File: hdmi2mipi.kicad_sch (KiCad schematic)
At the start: 1 part

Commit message: Add RP2040, fix pinout, add transistors for controlling the 1.8v and 3.3v outputs on the MIPI connector
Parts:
- added C1, C15, C2: 22p, Capacitor_SMD:C_0402_1005Metric, symbol mch2021-rescue:C-Device
- added C10, C11, C12, C13, C14, C4, C5, C6, C7: 100n, Capacitor_SMD:C_0402_1005Metric, symbol mch2021-rescue:C-Device
- added C16, C17, C8: 22u, Capacitor_SMD:C_0805_2012Metric, symbol mch2021-rescue:C-Device
- added C3, C9: 1u, Capacitor_SMD:C_0402_1005Metric, symbol mch2021-rescue:C-Device
- added C6: ~, symbol Device:C_Small
- added D1, D2, D3, D4, D5: LED, LED_SMD:LED_0603_1608Metric, symbol Device:LED
- added H1, H2, H3, H4: MountingHole_Pad, MountingHole:MountingHole_2.2mm_M2_Pad_Via, symbol Mechanical:MountingHole_Pad
- added J10: BOOT, Connector_PinHeader_2.54mm:PinHeader_1x02_P2.54mm_Vertical, symbol Connector_Generic:Conn_01x02
- added J11: USB_C_Receptacle_USB2.0, Connector_USB:USB_C_Receptacle_HRO_TYPE-C-31-M-12, symbol Connector:USB_C_Receptacle_USB2.0
- added J2: HDMI_A_1.4, symbol Connector:HDMI_A_1.4
- added J3: ~, symbol tc358870xbg:Conn_01x60_mipi_pinout
- added J6: QWIIC, symbol Connector_Generic_MountingPin:Conn_01x04_MountingPin
- added J7: SWD, Connector_JST:JST_SH_SM03B-SRSS-TB_1x03-1MP_P1.00mm_Horizontal, symbol Connector_Generic_MountingPin:Conn_01x03_MountingPin
- added J7: TP, Connector_JST:JST_SH_SM07B-SRSS-TB_1x07-1MP_P1.00mm_Horizontal, symbol Connector_Generic_MountingPin:Conn_01x07_MountingPin
- added L1: 2.2u, custom:Inductor_MSC20FC, symbol mch2021-rescue:L-Device
- added Q1, Q2, Q3 (x4): BC846, Package_TO_SOT_SMD:SOT-23, symbol Transistor_BJT:BC846
- added R10, R11, R12, R13, R18, R5, R8, R9: 1k, Resistor_SMD:R_0402_1005Metric, symbol mch2021-rescue:R-Device
- added R10: 2k, symbol Device:R_Small
- added R11: 48k, symbol Device:R_Small
- added R12: 0, symbol Device:R_Small
- added R13: 1.5k, symbol Device:R_Small
- added R14, R15: 5.1k, Resistor_SMD:R_0402_1005Metric, symbol mch2021-rescue:R-Device
- added R14, R20, R21, R23, R24, R25, R26, R27, R28, R29, R41, R43, R45, R47, R48: 4.7k, symbol Device:R_Small
- added R15, R38, R39, R40, R42, R44, R46, R49, R50: 10k, symbol Device:R_Small
- added R16, R17, R37: 33, symbol Device:R_Small
- added R16: 10k, Resistor_SMD:R_0402_1005Metric, symbol mch2021-rescue:R-Device
- added R17: 45.3k, Resistor_SMD:R_0402_1005Metric, symbol mch2021-rescue:R-Device
- added R18, R19: 1k, symbol Device:R_Small
- added R22: 100k, symbol Device:R_Small
- added R5 (x2): 100, Resistor_SMD:R_0402_1005Metric, symbol mch2021-rescue:R-Device
- added R6, R7: 27, Resistor_SMD:R_0402_1005Metric, symbol mch2021-rescue:R_Small-Device
- added U1: RP2040, custom:QFN40P700X700X90-57N, symbol RP2040:RP2040
- added U2: W25Q16JVUXIQ, custom:PSON50P300X200X60-9N, symbol mch2021-rescue:SPIFLASH_QSPI-spiflash
- added U3: W25Q16JVUXIQ, Package_SO:SOIC-8_5.23x5.23mm_P1.27mm, symbol mch2021-rescue:SPIFLASH_QSPI-spiflash
- added U3 (x2): SY6280AAC, Package_TO_SOT_SMD:SOT-23-5, symbol symbols:AAT4610BIGV-1-T1-Power_Management
- added U4: PCA9306DC, Package_SO:VSSOP-8_2.3x2mm_P0.5mm, symbol Interface:PCA9306DC
- added U4: SY8079AAC, Package_TO_SOT_SMD:SOT-23-5, symbol mch2021-rescue:TLV62568DBV-Regulator_Switching
- added X2: SG-210STF, Oscillator:Oscillator_SMD_SeikoEpson_SG210-4Pin_2.5x2.0mm, symbol Oscillator:SG-210STF
- added Y1: 12MHz, Crystal:Crystal_SMD_3225-4Pin_3.2x2.5mm, symbol mch2021-rescue:Crystal_GND24_Small-Device
- renumbered U1 to U2
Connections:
- net VDDC11 is gone; now on net VDD11_HDMI: U2.C10 (VDDC11), U2.K6 (VDDC11)
- net GND: now also U2.G5 (TEST), C1.2, C10.2, C11.2, C12.2, C13.2, C14.2, C16.2, C17.2, C2.2, C3.2, C4.2, C5.2, C6.2, C6.2, C7.2, C8.2, C9.2, D1.1 (K), D2.1 (K), D3.1 (K), D4.1 (K), D5.1 (K), H1.1, H2.1, H3.1, H4.1, J10.1 (Pin_1), J11.A1 (GND), J11.A12 (GND), J11.B1 (GND), J11.B12 (GND), J11.S1 (SHIELD), J2.11 (CKS), J2.17 (GND), J2.2 (D2S), J2.5 (D1S), J2.8 (D0S), J2.SH, J3.1 (GND), J3.10 (GND), J3.13 (GND), J3.16 (GND), J3.19 (GND), J3.22 (GND), J3.25 (GND), J3.28 (GND), J3.31 (GND), J3.4 (GND), J3.44 (GND), J3.46 (GND), J3.49 (GND), J3.7 (GND), J6.1 (Pin_1), J6.MP (MountPin), J7.2 (Pin_2), J7.7 (Pin_7), J7.MP (MountPin), J7.MP (MountPin), Q1.2 (E), Q2.2 (E), Q3.2 (E), Q3.2 (E), Q3.2 (E), Q3.2 (E), R11.1, R14.1, R15.1, R16.2, R22.1, R23.2, R38.2, R39.2, R40.2, R42.2, R44.2, R46.2, R48.2, R49.2, R50.2, U1.19 (TESTEN), U1.57 (GND), U2.4 (VSS), U3.2 (GND), U3.2 (GND), U3.4 (VSS), U4.1 (GND), U4.2 (GND), X2.2 (GND), Y1.2, Y1.4
- net VDD33_HDMI: now also U2.H2 (VDDIO33), U2.J7 (VDDIO18), R10.2, R27.1, R29.1, U3.1 (OUT), X2.1 (~{ST}), X2.4 (Vcc)
- net at U2.A1 (REXT): now also R10.1
- net at U2.A2 (CEC): now also J2.13 (CEC)
- net at U2.A3 (DDC_SCL): now also R16.1
- net at U2.A4 (HPDI): now also R12.2, R13.1
- net at U2.A5 (CDSI1D3P): now also J3.3 (DSI1D3P)
- net at U2.A6 (CDSI1D2P): now also J3.6 (DSI1D2P)
- net at U2.A7 (CDSI1CP): now also J3.9 (DSI1CP)
- net at U2.A8 (CDSI1D1P): now also J3.12 (DSID1P)
- net at U2.A9 (CDSI1D0P): now also J3.15 (DSI1D0P)
- net MC_VSUPPLY_12: now reaches U2.B10 (VDD12_MIPI1)
- net MC_VSUPPLY_12: now also U2.J10 (VDD12_MIPI0)
- net at U2.B3 (DDC_SDA): now also R17.2
- net at U2.B4 (HPDO): now also R14.2, R18.1
- net at U2.B5 (CDSI1D3N): now also J3.2 (DSI1D3N)
- net at U2.B6 (CDSI1D2N): now also J3.5 (DSI1D2N)
- net at U2.B7 (CDSI1CN): now also J3.8 (DSI1CN)
- net at U2.B8 (CDSI1D1N): now also J3.11 (DSID1N)
- net at U2.B9 (CDSI1D0N): now also J3.14 (DSI1D0N)
- net at U2.C1 (HDMICP): now also J2.10 (CK+)
- net at U2.C2 (HDMICN): now also J2.12 (CK-)
- net at U2.D1 (HDMID0P): now also J2.7 (D0+)
- net at U2.D10 (CDSI0D3P): now also J3.18 (DSI0D3P)
- net at U2.D2 (HDMID0N): now also J2.9 (D0-)
- net at U2.D9 (CDSI0D3N): now also J3.17 (DSI0D3N)
- net at U2.E1 (HDMID1P): now also J2.4 (D1+)
- net at U2.E10 (CDSI0D2P): now also J3.21 (DSI0D2P)
- net at U2.E2 (HDMID1N): now also J2.6 (D1-)
- net at U2.E9 (CDSI0D2N): now also J3.20 (DSI0D2N)
- net at U2.F1 (HDMID2P): now also J2.1 (D2+)
- net at U2.F10 (CDSI0CP): now also J3.24 (DSI0CP)
- net at U2.F2 (HDMID2N): now also J2.3 (D2-)
- net at U2.F9 (CDSI0CN): now also J3.23 (DSI0CN)
- net at U2.G10 (CDSI0D1P): now also J3.27 (DSI0D1P)
- net at U2.G9 (CDSI0D1N): now also J3.26 (DSI0D1N)
- net at U2.H10 (CDSI0D0P): now also J3.30 (DSI0D0P)
- net at U2.H9 (CDSI0D0N): now also J3.29 (DSI0D0N)
- net at U2.J3 (INT): now also R40.1, U1.40 (GPIO28/ADC2)
- net at U2.K3 (I2C_SDA): now also R29.2, U1.36 (GPIO24)
- net at U2.K4 (I2C_SCL): now also R27.2, U1.37 (GPIO25)
- net at U2.K8 (~{RESET}): now also R38.1, U1.39 (GPIO27/ADC1)
- net at U2.K9 (REFCLK): now also R37.2
- new net: D4.2 (A), R12.2
- new net: J2.18 (+5V), R12.1, R15.1, R20.1, R21.1, R22.2
- new net: Q1.3 (C), Q2.1 (B), R15.2
- new net: J7.3 (Pin_3), R24.2, U4.3 (SCL1)
- new net: C2.1, R5.1, Y1.3
- new net: J2.19 (HPD/HEAC-), Q2.3 (C), R18.2, R19.1
- new net: D2.2 (A), R10.2
- new net: J2.15 (SCL), R16.2, R21.2
- new net: Q1.1 (B), R14.1
- new net: C6.1, R11.2, R13.2, R19.2
- new net: J7.4 (Pin_4), R25.2, U4.4 (SDA1)
- new net: J6.3 (Pin_3), R26.2, U1.34 (GPIO22), U4.5 (SDA2)
- new net: J6.4 (Pin_4), R28.2, U1.35 (GPIO23), U4.6 (SCL2)
- new net: J11.A7 (D-), J11.B7 (D-), R6.1
- new net: R6.2, U1.46 (USB_DM)
- new net: D1.2 (A), R9.2
- new net: R49.1, U1.5 (GPIO3), U3.4 (ON)
- new net: J7.1 (Pin_1), R5.1
- new net: J7.3 (Pin_3), R5.1
- new net: Q3.1 (B), R46.1, U1.3 (GPIO1)
- new net: J3.41 (1.8-S1), Q3.3 (C), R47.2
- new net: R48.1, U3.3 (SET)
- new net: R50.1, U1.38 (GPIO26/ADC0), U3.4 (ON)
- new net: D5.2 (A), R13.2
- new net: Q3.1 (B), R44.1, U1.4 (GPIO2)
- new net: J3.33 (3.3-S1), Q3.3 (C), R43.2
- new net: J3.34 (3.3-S2), Q3.3 (C), R41.2
- new net: J3.36 (3.3v), J3.37 (3.3v), R41.1, R43.1, U3.1 (OUT)
- new net: J3.39 (1.8v), R45.1, R47.1
- new net: J3.42 (1.8-S2), Q3.3 (C), R45.2
- new net: J3.51 (LED+), J3.52 (LED+), J3.53 (LED+)
- new net: J3.55 (FB2), J3.56 (FB2)
- new net: J3.59 (FB1), J3.60 (FB1)
- new net: J2.16 (SDA), R17.1, R20.2
- new net: R5.2, U1.25 (SWD)
- new net: J11.A5 (CC1), R14.2
- new net: Q3.1 (B), R39.1, U1.7 (GPIO5)
- new net: D3.2 (A), R11.2
- new net: R18.1, U1.26 (RUN)
- new net: R5.2, U1.24 (SWCLK)
- new net: R7.1, U1.47 (USB_DP)
- new net: Q3.1 (B), R42.1, U1.6 (GPIO4)
- new net: R23.1, U3.3 (SET)
- new net: J11.A6 (D+), J11.B6 (D+), R7.2
- new net: J11.B5 (CC2), R15.2
- new net: R37.1, X2.3 (OUT)
- new net +3V3: C10.1, C12.1, C14.1, C15.1, C16.1, C17.1, C3.1, C4.1, C5.1, C7.1, J6.2 (Pin_2), L1.1, R17.1, R18.2, R26.1, R28.1, U1.1 (IOVDD), U1.10 (IOVDD), U1.22 (IOVDD), U1.33 (IOVDD), U1.42 (IOVDD), U1.43 (ADC_AVDD), U1.44 (VREG_VIN), U1.48 (USB_VDD), U1.49 (IOVDD), U2.8 (VDD), U3.5 (IN), U3.5 (IN), U3.8 (VDD), U4.7 (VREF2), U4.8 (EN)
- new net FB33: C15.2, R16.1, R17.2, U4.5 (FB)
- new net RP_BTN: J10.2 (Pin_2), R8.2
- new net RP_QSPI_CSN: R8.1, U1.56 (QSPI_CSN), U2.1 (~{CS}), U3.1 (~{CS})
- new net RP_QSPI_SCLK: U1.52 (QSPI_SCLK), U2.6 (SCK), U3.6 (SCK)
- new net RP_QSPI_SD0: U1.53 (QSPI_SD0), U2.5 (MOSI/IO0), U3.5 (MOSI/IO0)
- new net RP_QSPI_SD1: U1.55 (QSPI_SD1), U2.2 (MISO/IO1), U3.2 (MISO/IO1)
- new net RP_QSPI_SD2: U1.54 (QSPI_SD2), U2.3 (IO2), U3.3 (IO2)
- new net RP_QSPI_SD3: U1.51 (QSPI_SD3), U2.7 (IO3), U3.7 (IO3)
- new net RP_XIN: C1.1, U1.20 (XIN), Y1.1
- new net RP_XOUT: R5.2, U1.21 (XOUT)
- new net SW33: L1.2, U4.3 (SW)
- new net TP_INT: J7.1 (Pin_1)
- new net TP_RST: J7.2 (Pin_2)
- new net TP_VSUPPLY_18: J7.5 (Pin_5), R24.1, R25.1, U4.2 (VREF1)
- new net TP_VSUPPLY_33: J7.6 (Pin_6)
- new net VIN: C6.1, C8.1, J11.A4 (VBUS), J11.A9 (VBUS), J11.B4 (VBUS), J11.B9 (VBUS), J3.35 (5v), U4.1 (EN), U4.4 (VIN)
- new net rpi_1.1v: C11.1, C13.1, C9.1, U1.23 (DVDD), U1.45 (VREG_VOUT), U1.50 (DVDD)
- no-connect marks 0 -> 11
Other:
- note added: "1.8v"
- note added: "100k pulldown to pull SDA/SCL low when HDMI is disconnected"
- note added: "3.3v"
- note added: "5v"
- note added: "?"
- note added: "GND"
- note added: "I2C0 SDA I2C0 SCL"
- note added: "I2C1 SDA I2C1 SCL"
- note added: "No clue yet how these are supposed to work"
- note added: "Place close to chip"
- note added: "Place close to pin 44"
- note added: "Place close to pin 45"
- note added: "Pulldown on INT: I2C address is 0x0F"
- note added: "SPI0 SCK SPI0 TX SPI0 RX"
- note added: "SPI1 SCK SPI1 TX SPI1 RX"
- note added: "To-do: add 1.8v DC-DC"
- note added: "UART0 TX UART0 RX UART0 CTS UART0 RTS"
- note added: "UART1 TX UART1 RX UART1 CTS UART1 RTS"
- company: (none) -> Nicolai Electronics
- title: (none) -> HDMI to MIPI converter

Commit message: Most of schematic done, experimenting with component placement
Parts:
- removed U3: SY6280AAC, Package_TO_SOT_SMD:SOT-23-5, symbol symbols:AAT4610BIGV-1-T1-Power_Management
- added C1: 1u, Capacitor_SMD:C_0402_1005Metric, symbol mch2021-rescue:C-Device
- added C14, C33, C4: 100n, Capacitor_SMD:C_0402_1005Metric, symbol Device:C_Small
- added C15 (x3): 22p, Capacitor_SMD:C_0402_1005Metric, symbol mch2021-rescue:C-Device
- added C16 (x3), C17 (x3), C8 (x4): 22u, Capacitor_SMD:C_0805_2012Metric, symbol mch2021-rescue:C-Device
- added C3, C6 (x7): 100n, Capacitor_SMD:C_0402_1005Metric, symbol mch2021-rescue:C-Device
- added C39, C43: 1n, Capacitor_SMD:C_0402_1005Metric, symbol Device:C_Small
- added C40, C41: 0.1u, Capacitor_SMD:C_0402_1005Metric, symbol Device:C_Small
- added C42: 5p, Capacitor_SMD:C_0402_1005Metric, symbol Device:C_Small
- added C47 (x2): 39n, Capacitor_SMD:C_0402_1005Metric, symbol Device:C_Small
- added C5, C6: 47u, Capacitor_SMD:C_0805_2012Metric, symbol Device:C_Small
- added J1: AudioJack3, custom:Boom-audiojack-PJ-320B, symbol mch2021-rescue:AudioJack3-Connector
- added L1 (x3): 2.2u, custom:Inductor_MSC20FC, symbol mch2021-rescue:L-Device
- added Q7: 2SC2712, Package_TO_SOT_SMD:SOT-23, symbol Device:Q_NPN_BEC
- added R16 (x6), R17: 10k, Resistor_SMD:R_0402_1005Metric, symbol mch2021-rescue:R-Device
- added R17: 20k, Resistor_SMD:R_0402_1005Metric, symbol mch2021-rescue:R-Device
- added R17: 8.2k, Resistor_SMD:R_0402_1005Metric, symbol mch2021-rescue:R-Device
- added R27, R28: 330, Resistor_SMD:R_0402_1005Metric, symbol mch2021-rescue:R-Device
- added R60: 1k, Resistor_SMD:R_0402_1005Metric, symbol Device:R_Small
- added U1: MS4344, custom:SOP50P490X110-10N, symbol CS4344-CZZ:CS4344-CZZ
- added U4 (x3): SY8079AAC, Package_TO_SOT_SMD:SOT-23-5, symbol mch2021-rescue:TLV62568DBV-Regulator_Switching
- C6: footprint (none) -> Capacitor_SMD:C_0402_1005Metric
- J2: footprint (none) -> Connector_HDMI:HDMI_A_Molex_208658-1001_Horizontal
- J3: footprint (none) -> fpc60:Hirose_FH52-60S-0.5SH_1x60-1MP_P0.50mm_Horizontal
- J5: renamed from J6; footprint (none) -> Connector_JST:JST_SH_SM04B-SRSS-TB_1x04-1MP_P1.00mm_Horizontal
- R10, R11, R12, R13, R14, R15, R16, R17, R18, R19, R20, R21, R22, R23, R24, R25, R26, R27, R28, R29, R37, R38, R39, R40, R41, R42, R43, R44, R45, R46, R47, R50: footprint (none) -> Resistor_SMD:R_0402_1005Metric
- R48: value 4.7k -> 1k; footprint (none) -> Resistor_SMD:R_0402_1005Metric
- R49: value 10k -> 1.5k; footprint (none) -> Resistor_SMD:R_0402_1005Metric
- renumbered J7 to J4, Q3 to Q4, Q3 to Q5, Q3 to Q6
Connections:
- net TP_VSUPPLY_18 is gone; now on net +1V8: J4.5 (Pin_5), R24.1, R25.1, U4.2 (VREF1)
- net TP_VSUPPLY_33 is gone; now on net VDD33_HDMI: J4.6 (Pin_6)
- net +3V3: now also C1.1, C3.1, U1.9 (VA)
- net GND: now also J3.12 (GND), J3.15 (GND), J3.17 (GND), J3.30 (GND), J3.33 (GND), J3.36 (GND), J3.39 (GND), J3.42 (GND), J3.45 (GND), J3.48 (GND), J3.51 (GND), J3.54 (GND), J3.57 (GND), J3.60 (GND), J3.MP, C1.2, C16.2, C16.2, C16.2, C17.2, C17.2, C17.2, C3.2, C39.2, C4.2, C40.2, C47.1, C47.1, C5.2, C6.2, C6.2, C6.2, C6.2, C6.2, C6.2, C6.2, C6.2, C8.2, C8.2, C8.2, C8.2, J1.S, R16.2, R16.2, R16.2, R16.2, R16.2, R16.2, U1.8 (GND), U4.2 (GND), U4.2 (GND), U4.2 (GND); no longer J3.1 (GND), J3.10 (GND), J3.13 (GND), J3.16 (GND), J3.19 (GND), J3.22 (GND), J3.25 (GND), J3.28 (GND), J3.31 (GND), J3.4 (GND), J3.44 (GND), J3.46 (GND), J3.49 (GND), J3.7 (GND), R48.2, R49.2
- net VDD33_HDMI: now also J3.24 (3.3v), J3.25 (3.3v), R41.1, R43.1, C6.1, C6.1, C8.1, Q7.3 (C)
- net VIN: now also J3.26 (5v); no longer C6.1, C8.1, J11.A4 (VBUS), J11.A9 (VBUS), J11.B4 (VBUS), J11.B9 (VBUS), J3.35 (5v), U4.1 (EN), U4.4 (VIN)
- net at J3.3: no longer U2.A5 (CDSI1D3P)
- net at J3.6 (FB2): now also J3.5 (FB2); no longer U2.A6 (CDSI1D2P)
- net at J3.9 (LED+): now also J3.10 (LED+), J3.8 (LED+); no longer U2.A7 (CDSI1CP)
- net DSI1_D1_P: now reaches U2.A8 (CDSI1D1P)
- net DSI1_D1_P: now also J3.49 (DSID1P); no longer J3.12 (DSID1P)
- net DSI1_D0_P: now reaches U2.A9 (CDSI1D0P)
- net DSI1_D0_P: now also J3.46 (DSI1D0P); no longer J3.15 (DSI1D0P)
- net at J3.2 (FB1): now also J3.1 (FB1); no longer U2.B5 (CDSI1D3N)
- net DSI1_D2_N: now reaches U2.B6 (CDSI1D2N)
- net DSI1_D2_N: now also J3.56 (DSI1D2N); no longer J3.5 (DSI1D2N)
- net DSI1_C_N: now reaches U2.B7 (CDSI1CN)
- net DSI1_C_N: now also J3.53 (DSI1CN); no longer J3.8 (DSI1CN)
- net at J3.11: no longer U2.B8 (CDSI1D1N)
- net at J3.14 (5.8v-VDD): no longer U2.B9 (CDSI1D0N)
- net HDMI_C_P: now reaches J2.10 (CK+), U2.C1 (HDMICP)
- net HDMI_C_N: now reaches J2.12 (CK-), U2.C2 (HDMICN)
- net HDMI_0_P: now reaches J2.7 (D0+), U2.D1 (HDMID0P)
- net at J3.18: no longer U2.D10 (CDSI0D3P)
- net HDMI_0_N: now reaches J2.9 (D0-), U2.D2 (HDMID0N)
- net DSI0_D3_N: now reaches U2.D9 (CDSI0D3N)
- net DSI0_D3_N: now also J3.44 (DSI0D3N); no longer J3.17 (DSI0D3N)
- net HDMI_1_P: now reaches J2.4 (D1+), U2.E1 (HDMID1P)
- net at J3.21: no longer U2.E10 (CDSI0D2P)
- net HDMI_1_N: now reaches J2.6 (D1-), U2.E2 (HDMID1N)
- net at J3.20 (1.8-S1): now also Q6.3 (C), R47.2; no longer U2.E9 (CDSI0D2N)
- net HDMI_2_P: now reaches J2.1 (D2+), U2.F1 (HDMID2P)
- net DSI0_C_P: now reaches U2.F10 (CDSI0CP)
- net DSI0_C_P: now also J3.37 (DSI0CP); no longer J3.24 (DSI0CP)
- net HDMI_2_N: now reaches J2.3 (D2-), U2.F2 (HDMID2N)
- net at J3.23: no longer U2.F9 (CDSI0CN)
- net at J3.27 (3.3-S2): now also Q3.3 (C), R41.2; no longer U2.G10 (CDSI0D1P)
- net DSI0_D1_N: now reaches U2.G9 (CDSI0D1N)
- net DSI0_D1_N: now also J3.35 (DSI0D1N); no longer J3.26 (DSI0D1N)
- net DSI0_D0_P: now reaches U2.H10 (CDSI0D0P)
- net DSI0_D0_P: now also J3.31 (DSI0D0P); no longer J3.30 (DSI0D0P)
- net at J3.29: no longer U2.H9 (CDSI0D0N)
- net at U2.J1 (BIASDA): now also C41.2
- net at U2.J2 (DAOUT): now also R49.2
- net at U2.J4 (A_OSCK): now also U1.4 (MCLK)
- net at U2.J9 (A_SD0): now also U1.1 (SDIN)
- net at U2.K1 (PCKIN): now also C43.2
- net at U2.K2 (PFIL): now also R48.1, C39.1
- net at U2.K5 (A_WFS): now also U1.3 (LRCK)
- net at U2.K7 (A_SCK): now also U1.2 (~{DEM}/SCLK)
- net at R10.1: now also U1.14 (GPIO11)
- net at R49.1: now also C42.1, Q7.1 (B); no longer U1.5 (GPIO3)
- net 1V8_S1: now reaches Q6.1 (B), R46.1
- net 1V8_S1: now also U1.2 (GPIO0); no longer U1.3 (GPIO1)
- net 1V8_S2: now reaches Q5.1 (B), R44.1
- net 1V8_S2: now also U1.3 (GPIO1); no longer U1.4 (GPIO2)
- net DSI0_D0_N: now reaches J3.32 (DSI0D0N)
- net DSI0_D0_N: now also U2.H9 (CDSI0D0N)
- net at Q4.3 (C), R43.2: now also J3.28 (3.3-S1); no longer J3.33 (3.3-S1)
- net DSI0_C_N: now reaches J3.38 (DSI0CN)
- net DSI0_C_N: now also U2.F9 (CDSI0CN)
- net +1V8: now reaches R45.1, R47.1
- net +1V8: now also J3.22 (1.8v), C15.1, C16.1, C17.1, L1.1, R17.1; no longer J3.39 (1.8v)
- net DSI0_D2_P: now reaches J3.40 (DSI0D2P)
- net DSI0_D2_P: now also U2.E10 (CDSI0D2P)
- net at Q5.3 (C), R45.2: now also J3.19 (1.8-S2); no longer J3.42 (1.8-S2)
- net DSI0_D3_P: now reaches J3.43 (DSI0D3P)
- net DSI0_D3_P: now also U2.D10 (CDSI0D3P)
- net DSI1_D0_N: now reaches J3.47 (DSI1D0N)
- net DSI1_D0_N: now also U2.B9 (CDSI1D0N)
- net DSI1_D1_N: now reaches J3.50 (DSID1N)
- net DSI1_D1_N: now also U2.B8 (CDSI1D1N)
- net DSI1_D2_P: now reaches J3.55 (DSI1D2P)
- net DSI1_D2_P: now also U2.A6 (CDSI1D2P); no longer J3.56 (FB2)
- net DSI1_D3_P: now reaches J3.58 (DSI1D3P)
- net DSI1_D3_P: now also U2.A5 (CDSI1D3P)
- net DSI1_D3_N: now reaches J3.59 (DSI1D3N)
- net DSI1_D3_N: now also U2.B5 (CDSI1D3N); no longer J3.60 (FB1)
- net at R12.1: now also U1.16 (GPIO13)
- net 3V3_S2: now reaches Q3.1 (B), R39.1
- net 3V3_S2: now also U1.5 (GPIO3); no longer U1.7 (GPIO5)
- net at R11.1: now also U1.15 (GPIO12)
- net at U1.13 (GPIO10): now also R9.1
- net at U1.17 (GPIO14): now also R13.1
- net 1V1_EN: now reaches U1.18 (GPIO15)
- net 1V1_EN: now also R16.1, U4.1 (EN)
- net 1V2_EN: now reaches U1.27 (GPIO16)
- net 1V2_EN: now also R16.1, U4.1 (EN)
- net 1V8_EN: now reaches U1.28 (GPIO17)
- net 1V8_EN: now also R16.1, U4.1 (EN)
- net 3V3_S1: now reaches Q4.1 (B), R42.1
- net 3V3_S1: now also U1.4 (GPIO2); no longer U1.6 (GPIO4)
- net MC_VSUPPLY_12 renamed +1V2
- net +1V2: now also C15.1, C16.1, C17.1, C6.1, L1.1, R17.1
- net VDD11_HDMI renamed +1V1
- net +1V1: now also C15.1, C16.1, C17.1, C6.1, L1.1, R17.1
- new net: C5.1, U1.6 (FILT+)
- new net: C4.1, C6.1, U1.5 (VQ)
- new net: C33.1, U1.10 (AOUTR)
- new net: C33.2, R28.1
- new net: C43.1, Q7.2 (E), R60.2
- new net: C41.1, C42.2, R60.1
- new net: C40.1, R48.2
- new net: C14.2, U1.7 (AOUTL)
- new net: C14.1, R27.1
- new net AUDIO_L: C47.2, J1.T, R27.2
- new net AUDIO_R: C47.2, J1.R, R28.2
- new net DSI0_D1_P: J3.34 (DSI0D1P), U2.G10 (CDSI0D1P)
- new net DSI0_D2_N: J3.41 (DSI0D2N), U2.E9 (CDSI0D2N)
- new net DSI1_C_P: J3.52 (DSI1CP), U2.A7 (CDSI1CP)
- new net FB11: C15.2, R16.1, R17.2, U4.5 (FB)
- new net FB12: C15.2, R16.1, R17.2, U4.5 (FB)
- new net FB18: C15.2, R16.1, R17.2, U4.5 (FB)
- new net SW11: L1.2, U4.3 (SW)
- new net SW12: L1.2, U4.3 (SW)
- new net SW18: L1.2, U4.3 (SW)
- new net VBUS: C6.1, C6.1, C6.1, C6.1, C8.1, C8.1, C8.1, C8.1, J11.A4 (VBUS), J11.A9 (VBUS), J11.B4 (VBUS), J11.B9 (VBUS), U4.1 (EN), U4.4 (VIN), U4.4 (VIN), U4.4 (VIN), U4.4 (VIN)
- no-connect marks 11 -> 14
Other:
- added sheet Untitled Sheet (untitled.kicad_sch)
- note removed: "To-do: add 1.8v DC-DC"
- moved on the sheet: C15, C16, C17, C6, C8, D1, D2, D3, D4, D5, L1, Q3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

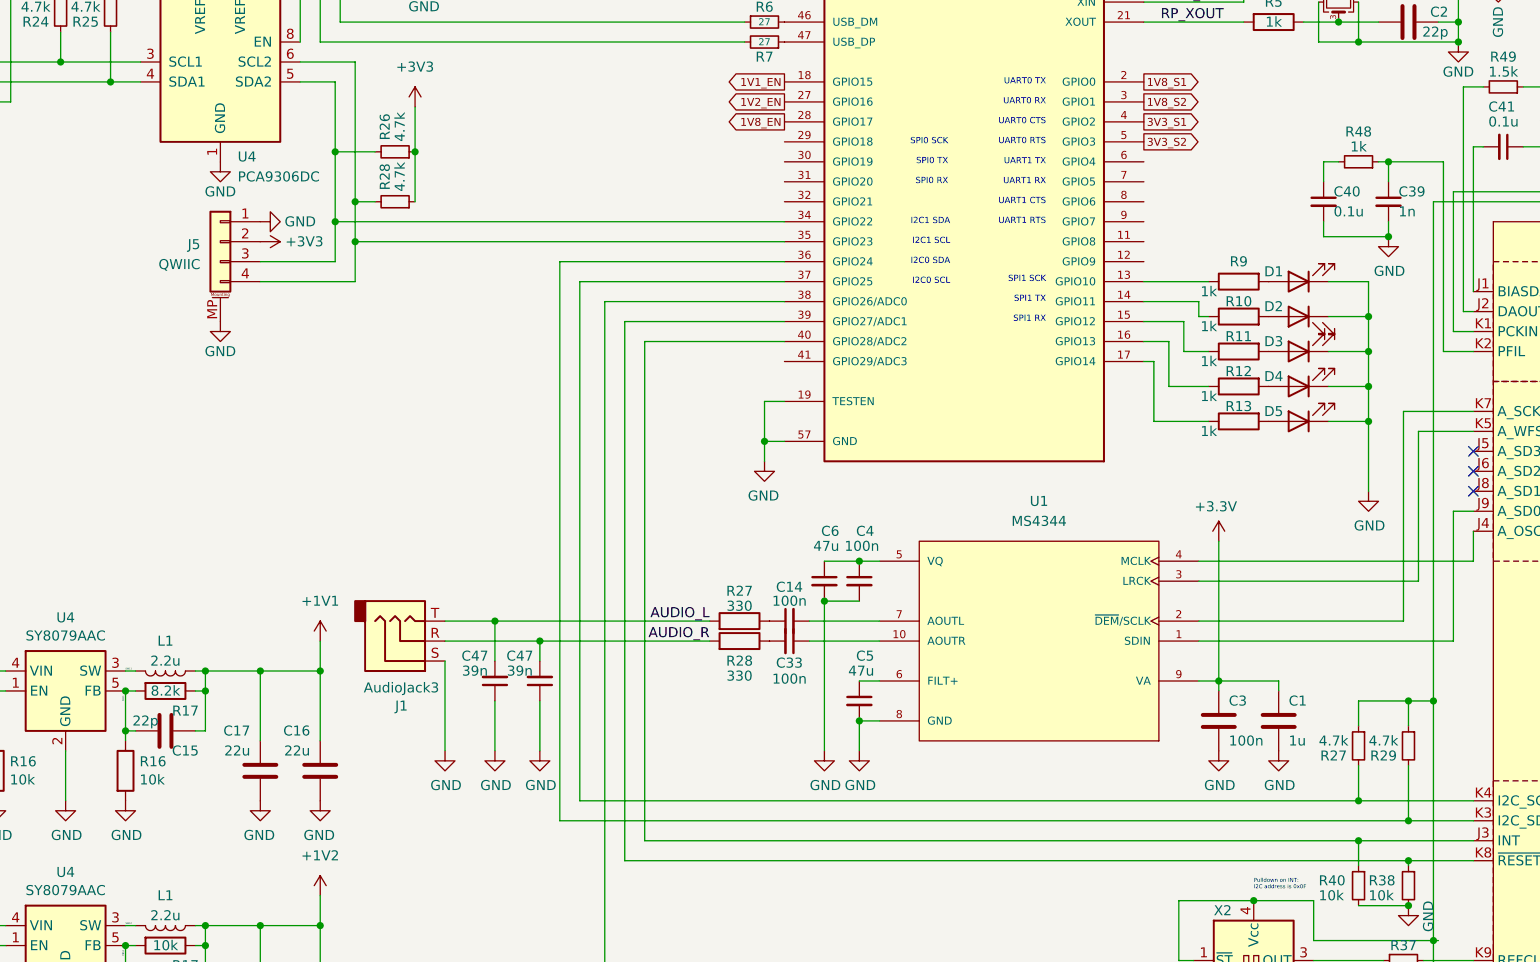
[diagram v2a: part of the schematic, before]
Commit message: Board to 7cm+-
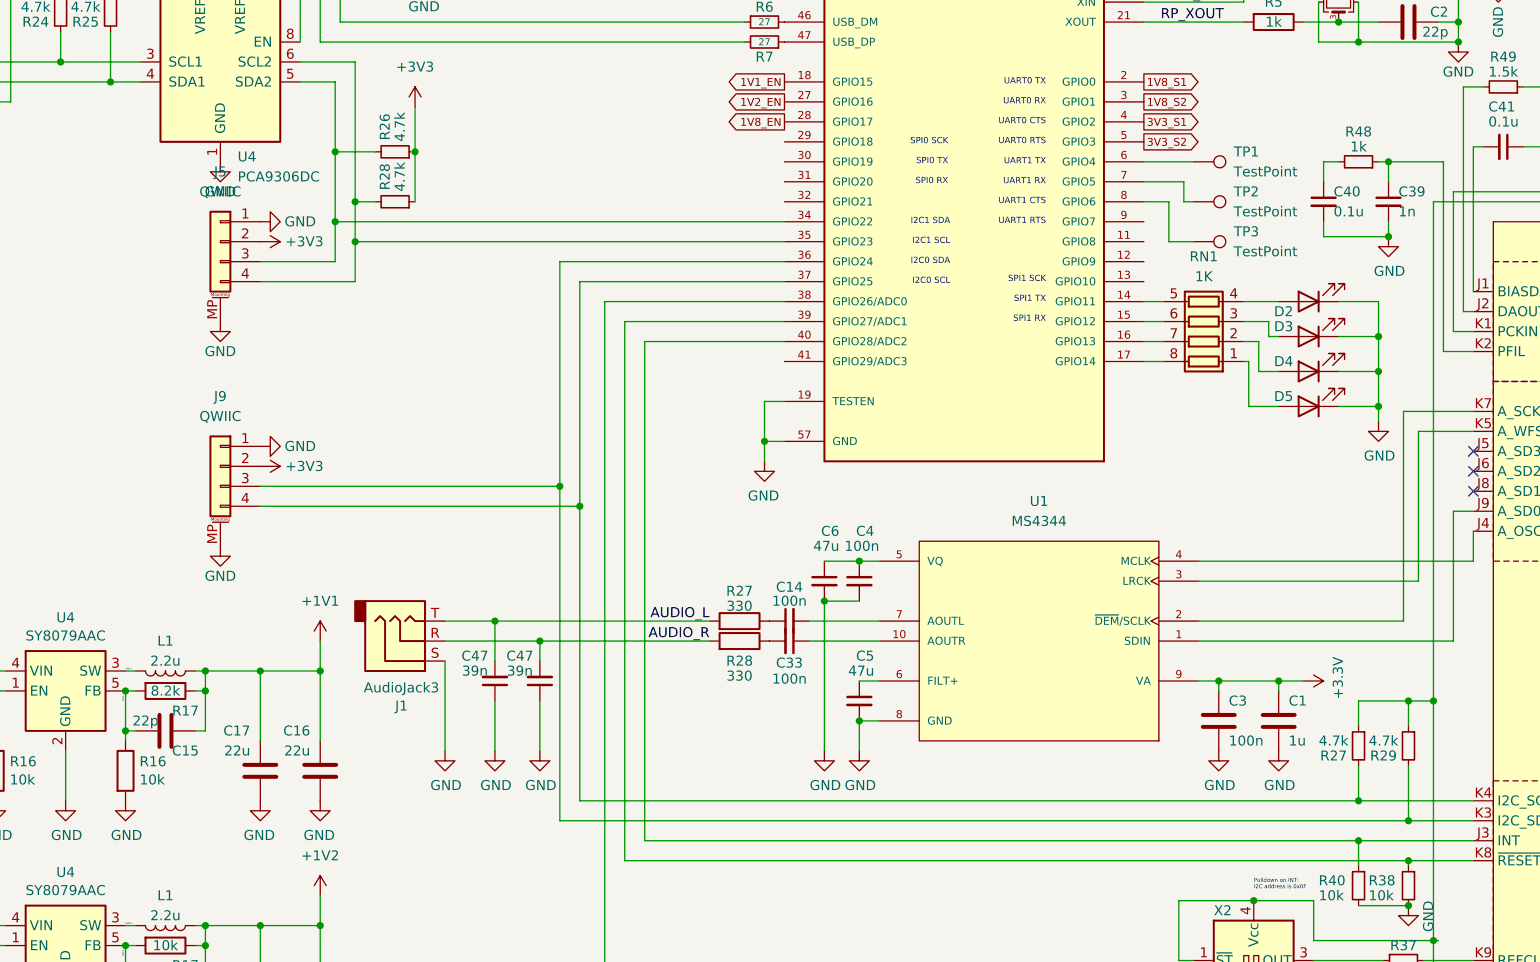
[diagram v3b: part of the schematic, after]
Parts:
- removed D1: LED, LED_SMD:LED_0603_1608Metric, symbol Device:LED
- removed R10, R11, R12, R13, R9: 1k, Resistor_SMD:R_0402_1005Metric, symbol mch2021-rescue:R-Device
- added J9: QWIIC, Connector_JST:JST_SH_SM04B-SRSS-TB_1x04-1MP_P1.00mm_Horizontal, symbol Connector_Generic_MountingPin:Conn_01x04_MountingPin
- added RN1: 1K, Resistor_SMD:R_Array_Convex_4x0402, symbol Device:R_Pack04
- added TP1, TP2, TP3: TestPoint, TestPoint:TestPoint_Pad_D1.0mm, symbol Connector:TestPoint
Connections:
- net +3V3: now also J9.2 (Pin_2)
- net GND: now also J9.1 (Pin_1), J9.MP (MountPin)
- net at R29.2, U1.36 (GPIO24), U2.K3 (I2C_SDA): now also J9.3 (Pin_3)
- net at R27.2, U1.37 (GPIO25), U2.K4 (I2C_SCL): now also J9.4 (Pin_4)
- net at D4.2 (A): now also RN1.2 (R2.1)
- net at U1.14 (GPIO11): now also RN1.5 (R4.2)
- net at D2.2 (A): now also RN1.4 (R4.1)
- net at D5.2 (A): now also RN1.1 (R1.1)
- net at U1.16 (GPIO13): now also RN1.7 (R2.2)
- net at U1.15 (GPIO12): now also RN1.6 (R3.2)
- net at D3.2 (A): now also RN1.3 (R3.1)
- net at U1.17 (GPIO14): now also RN1.8 (R1.2)
- net at U1.6 (GPIO4): now also TP1.1
- net at U1.7 (GPIO5): now also TP2.1
- net at U1.8 (GPIO6): now also TP3.1
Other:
- moved on the sheet: D2, D3, D4, D5
